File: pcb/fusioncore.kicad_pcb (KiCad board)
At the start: 2 copper layers, 95 x 99 mm, 107 parts, among them J1 Conn_02x12_Top_Bottom, J10 Pump_Misc_1, J11 Pump_Misc_2, J12 Flow_Warm, J13 Flow_Cold, J14 Trigger, J15 Valve_M1, J16 Valve_M2, J17 Valve_M3, J18 Valve_M4, J19 Valve_Air_Lime, J2 Temp_1, J20 Valve_Air_Rum, J21 Valve_Air_Out, J22 LED, J3 40HAT, J4 Temp_2, J5 WEIGHT, J6 Pump_Water_Cold, J7 Pump_Water_Warm, J8 Pump_Air, J9 CONN_01X02, Q1 DMG2305UX, Q10 AO3400A, Q11 AO3400A, Q12 AO3400A, Q13 AO3400A, Q14 AO3400A, Q15 BSS138, Q16 S8550, Q17 AO3400A, Q18 AO3400A, Q2 DMMT5401, Q3 AO3400A, Q4 AO3400A, Q5 AO3400A, Q6 AO3400A, Q7 AO3400A, Q8 AO3400A, Q9 AO3400A, U1 HX711, U2 CAT24C32, U3 LTC2990, U4 LTC2990

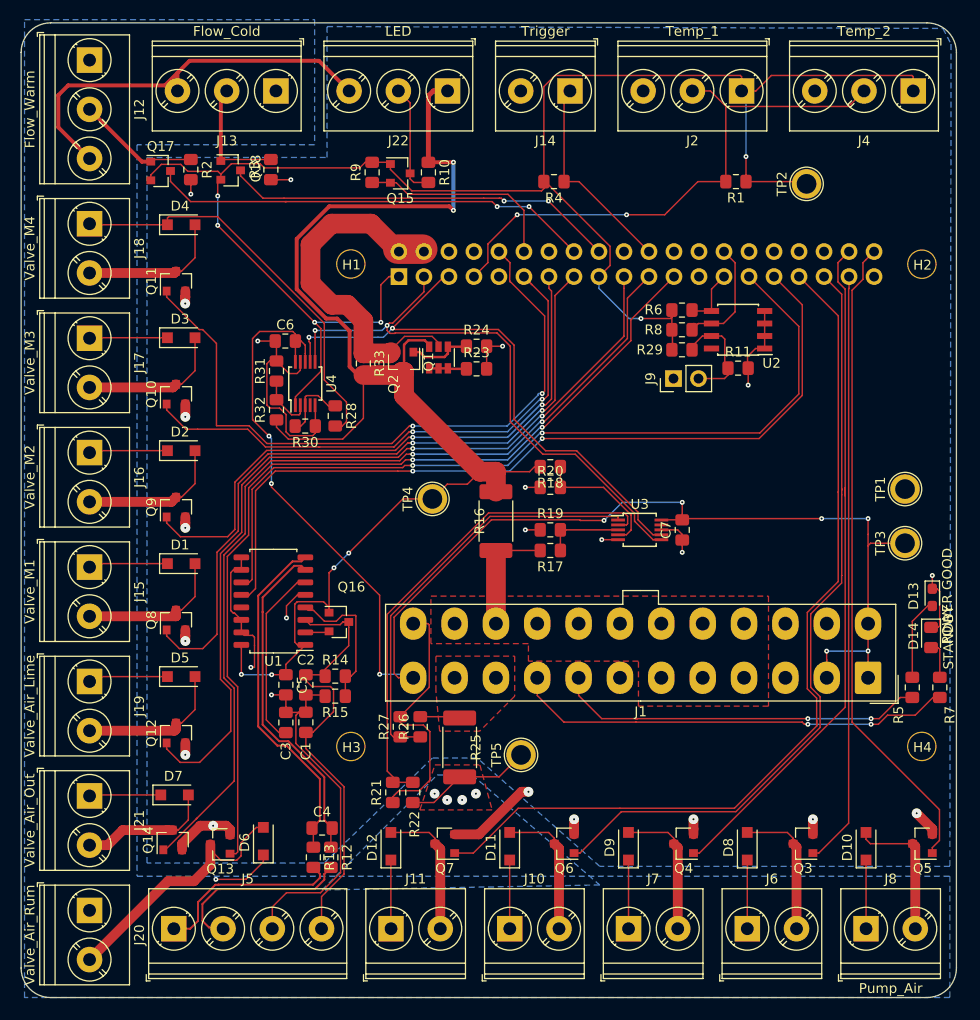
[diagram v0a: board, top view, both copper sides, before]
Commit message: Increased the number of vias for 12V power supply
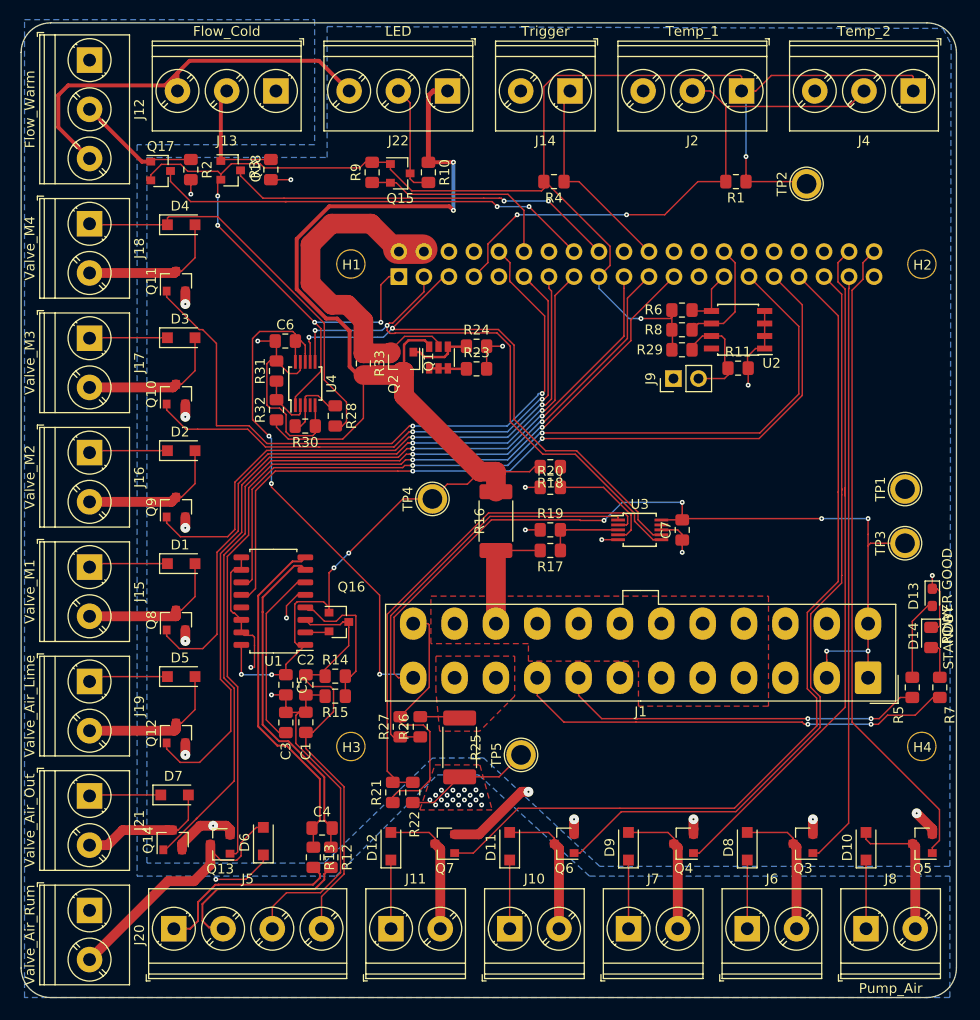
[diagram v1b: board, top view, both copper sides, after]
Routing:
- net /12V: vias 5 -> 20
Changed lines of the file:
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@@
     (thickness 1.6)
     (drawings 53)
-    (tracks 1091)
+    (tracks 1101)
     (zones 0)
     (modules 107)
@@
   )
   (page A4)
+  (title_block
+    (title "FusionCore Expansion")
+    (date 04.01.2020)
+    (rev A)
+    (company JKO)
+  )
   (layers
     (0 F.Cu signal)
-    (31 B.Cu signal hide)
+    (31 B.Cu signal)
     (32 B.Adhes user)
     (33 F.Adhes user)
@@
     (pad_to_mask_clearance 0.1)
     (aux_axis_origin 0 0)
-    (grid_origin 60.325 52.1716)
     (visible_elements 7FFFFE3F)
     (pcbplotparams
-      (layerselection 0x010f8_80000007)
+      (layerselection 0x010f0_ffffffff)
       (usegerberextensions false)
       (usegerberattributes false)
@@
       (drillshape 0)
       (scaleselection 1)
-      (outputdirectory "prod"))
+      (outputdirectory "gerber"))
   )
   (net 0 "")
@@
   (segment (start 72.252489 102.224489) (end 72.252489 103.063569) (width 0.15) (layer F.Cu) (net 1))
   (segment (start 72.252489 103.063569) (end 72.252489 105.283) (width 0.15) (layer F.Cu) (net 1))
-  (segment (start 65.228 101.480108) (end 65.228 102.080108) (width 1) (layer F.Cu) (net 1))
-  (segment (start 65.228 102.080108) (end 65.228 102.6025) (width 1) (layer F.Cu) (net 1))
   (segment (start 65.228 102.6025) (end 65.228 102.6025) (width 1) (layer F.Cu) (net 1))
   (via (at 65.228 102.6025) (size 1) (drill 0.2) (layers F.Cu B.Cu) (net 1))
-  (segment (start 65.228 90.00722) (end 65.228 90.60722) (width 1) (layer F.Cu) (net 1))
-  (segment (start 65.228 90.60722) (end 65.228 91.109) (width 1) (layer F.Cu) (net 1))
   (segment (start 65.228 91.109) (end 65.228 91.109) (width 1) (layer F.Cu) (net 1))
   (via (at 65.228 91.109) (size 1) (drill 0.2) (layers F.Cu B.Cu) (net 1))
@@
   (segment (start 65.228 79.833) (end 65.228 79.833) (width 1) (layer F.Cu) (net 1))
   (via (at 65.228 79.833) (size 1) (drill 0.2) (layers F.Cu B.Cu) (net 1))
-  (segment (start 65.228 67.661444) (end 65.2145 67.674944) (width 1) (layer F.Cu) (net 1))
-  (segment (start 65.2145 67.674944) (end 65.2145 68.326) (width 1) (layer F.Cu) (net 1))
-  (segment (start 65.228 67.061444) (end 65.228 67.661444) (width 1) (layer F.Cu) (net 1))
-  (segment (start 65.2145 68.326) (end 65.2145 68.326) (width 1) (layer F.Cu) (net 1))
-  (via (at 65.2145 68.326) (size 1) (drill 0.2) (layers F.Cu B.Cu) (net 1))
+  (via (at 65.2272 68.3768) (size 1) (drill 0.2) (layers F.Cu B.Cu) (net 1))
   (segment (start 74.614 55.748) (end 74.619 55.753) (width 0.15) (layer F.Cu) (net 1))
   (segment (start 73.914 55.748) (end 74.614 55.748) (width 0.15) (layer F.Cu) (net 1))
@@
   (segment (start 52.325 50.427) (end 55.499 53.601) (width 0.4) (layer F.Cu) (net 1))
   (segment (start 63.156923 46.1716) (end 53.325 46.1716) (width 0.4) (layer F.Cu) (net 1))
+  (segment (start 65.228 67.061444) (end 65.228 68.3776) (width 1) (layer F.Cu) (net 1))
+  (segment (start 65.228 91.109) (end 65.228 90.00722) (width 1) (layer F.Cu) (net 1))
+  (segment (start 65.228 102.6025) (end 65.228 101.480108) (width 1) (layer F.Cu) (net 1))
   (segment (start 119.94 66.06) (end 119.94 65.59) (width 0.25) (layer B.Cu) (net 2) (status 30))
   (segment (start 116.965 69.184) (end 116.77 68.989) (width 0.15) (layer F.Cu) (net 2) (status 30))
@@
   (segment (start 87.325 88.1716) (end 90.325 88.1716) (width 0.15) (layer F.Cu) (net 8))
   (segment (start 81.825 93.6716) (end 87.325 88.1716) (width 0.15) (layer F.Cu) (net 8))
-  (via (at 90.551 118.11) (size 1) (drill 0.2) (layers F.Cu B.Cu) (net 9))
-  (via (at 91.821 118.745) (size 1) (drill 0.2) (layers F.Cu B.Cu) (net 9))
-  (via (at 93.345 118.745) (size 1) (drill 0.2) (layers F.Cu B.Cu) (net 9))
-  (via (at 94.742 118.11) (size 1) (drill 0.2) (layers F.Cu B.Cu) (net 9))
-  (segment (start 90.4815 119.008) (end 93.091 116.3985) (width 0.15) (layer F.Cu) (net 9))
-  (segment (start 88.3285 119.008) (end 90.4815 119.008) (width 0.15) (layer F.Cu) (net 9))
   (segment (start 134.366 125.547) (end 134.366 131.826) (width 0.15) (layer F.Cu) (net 9))
   (segment (start 134.366 124.847) (end 134.366 125.547) (width 0.15) (layer F.Cu) (net 9))
@@
   (segment (start 63.538001 59.499999) (end 63.413 59.625) (width 0.15) (layer F.Cu) (net 9))
   (segment (start 68.51032 59.499999) (end 63.538001 59.499999) (width 0.15) (layer F.Cu) (net 9))
-  (segment (start 97.0981 116.3985) (end 99.325 114.1716) (width 0.15) (layer F.Cu) (net 9))
-  (segment (start 93.091 116.3985) (end 97.0981 116.3985) (width 0.15) (layer F.Cu) (net 9))
+  (via (at 95.3262 119.253) (size 0.5) (drill 0.2) (layers F.Cu B.Cu) (net 9))
+  (via (at 94.742 118.745) (size 0.5) (drill 0.2) (layers F.Cu B.Cu) (net 9))
+  (via (at 94.1578 119.253) (size 0.5) (drill 0.2) (layers F.Cu B.Cu) (net 9))
+  (via (at 93.5736 118.745) (size 0.5) (drill 0.2) (layers F.Cu B.Cu) (net 9))
+  (via (at 92.9894 119.253) (size 0.5) (drill 0.2) (layers F.Cu B.Cu) (net 9))
+  (via (at 92.4052 118.745) (size 0.5) (drill 0.2) (layers F.Cu B.Cu) (net 9))
+  (via (at 91.821 119.253) (size 0.5) (drill 0.2) (layers F.Cu B.Cu) (net 9))
+  (via (at 91.2368 118.745) (size 0.5) (drill 0.2) (layers F.Cu B.Cu) (net 9))
+  (via (at 90.6526 119.253) (size 0.5) (drill 0.2) (layers F.Cu B.Cu) (net 9))
+  (via (at 90.0684 118.745) (size 0.5) (drill 0.2) (layers F.Cu B.Cu) (net 9))
+  (via (at 94.1578 118.2624) (size 0.5) (drill 0.2) (layers F.Cu B.Cu) (net 9))
+  (via (at 92.9894 118.2624) (size 0.5) (drill 0.2) (layers F.Cu B.Cu) (net 9))
+  (via (at 91.821 118.2624) (size 0.5) (drill 0.2) (layers F.Cu B.Cu) (net 9))
+  (via (at 90.6526 118.2624) (size 0.5) (drill 0.2) (layers F.Cu B.Cu) (net 9))
+  (via (at 91.2368 117.7544) (size 0.5) (drill 0.2) (layers F.Cu B.Cu) (net 9))
+  (via (at 92.4052 117.7544) (size 0.5) (drill 0.2) (layers F.Cu B.Cu) (net 9))
+  (via (at 93.5736 117.729) (size 0.5) (drill 0.2) (layers F.Cu B.Cu) (net 9))
+  (via (at 94.742 117.729) (size 0.5) (drill 0.2) (layers F.Cu B.Cu) (net 9))
+  (via (at 95.3262 118.2624) (size 0.5) (drill 0.2) (layers F.Cu B.Cu) (net 9))
+  (segment (start 90.4815 119.008) (end 93.091 116.3985) (width 0.15) (layer F.Cu) (net 9))
+  (segment (start 88.3285 119.008) (end 90.4815 119.008) (width 0.15) (layer F.Cu) (net 9))
+  (segment (start 97.0981 116.3985) (end 93.091 116.3985) (width 0.15) (layer F.Cu) (net 9))
+  (segment (start 99.325 114.1716) (end 97.0981 116.3985) (width 0.15) (layer F.Cu) (net 9))
   (via (at 68.516001 57.404) (size 0.5) (drill 0.2) (layers F.Cu B.Cu) (net 10))
   (via (at 111.506 69.85) (size 0.5) (drill 0.2) (layers F.Cu B.Cu) (net 10))
@@
     (connect_pads (clearance 0.4))
     (min_thickness 0.254)
-    (fill yes (arc_segments 32) (thermal_gap 0.508) (thermal_bridge_width 0.508) (smoothing fillet) (radius 2))
-    (polygon
-      (pts
-        (xy 78.359 52.197) (xy 60.325 52.197) (xy 60.325 126.492) (xy 142.875 126.492) (xy 142.875 138.811)
-        (xy 48.895 138.811) (xy 48.895 39.497) (xy 78.359 39.497)
-      )
-    )
-  )
-  (zone (net 9) (net_name /12V) (layer B.Cu) (hatch edge 0.508)
-    (connect_pads (clearance 0.4))
-    (min_thickness 0.254)
     (fill yes (arc_segments 32) (thermal_gap 0.508) (thermal_bridge_width 0.508) (smoothing fillet) (radius 1))
     (polygon
       (pts
-        (xy 107.315 127.381) (xy 79.121 127.889) (xy 90.805 116.205) (xy 94.361 116.205)
+        (xy 78.359 52.197) (xy 60.325 52.197) (xy 60.325 126.492) (xy 80.518 126.492) (xy 90.805 116.205)
+        (xy 95.0214 116.205) (xy 106.284568 126.492) (xy 142.875 126.492) (xy 142.875 138.811) (xy 48.895 138.811)
+        (xy 48.895 39.497) (xy 78.359 39.497)
       )
     )
@@
     (polygon
       (pts
-        (xy 143.002 41.9735) (xy 142.875 125.492) (xy 107.325 125.492) (xy 94.875 114.492) (xy 90.325 114.492)
+        (xy 143.002 41.9735) (xy 142.875 125.492) (xy 107.325 125.492) (xy 95.5294 114.4778) (xy 90.325 114.492)
         (xy 79.325 125.1585) (xy 61.325 125.158497) (xy 61.325 53.492) (xy 79.629 53.492) (xy 79.629 40.1955)
         (xy 142.1765 40.386)

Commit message: Fixed component sizes and rearranged components to match spec
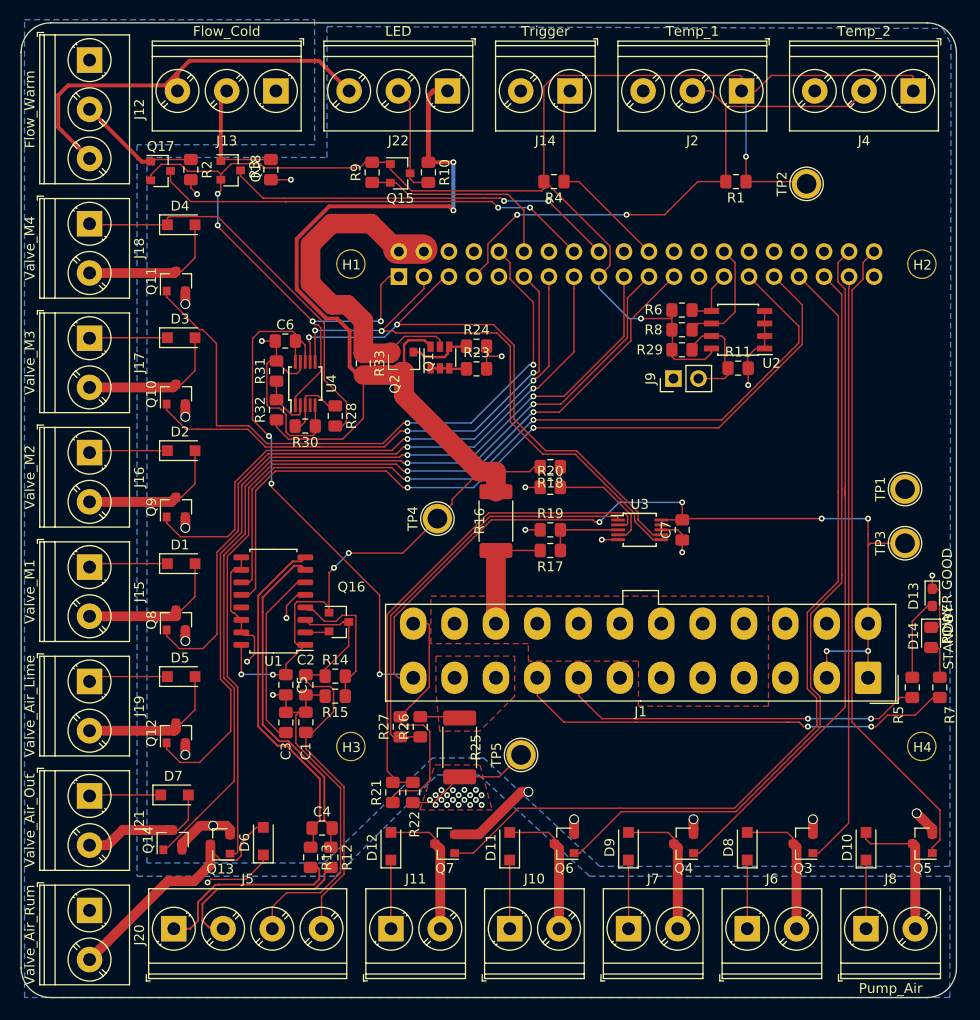
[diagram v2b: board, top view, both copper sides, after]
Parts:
- moved TP4 2.06 mm to (90.8, 90.2)
- moved R13 0.28 mm to (78.0, 124.6)
- moved Q2 0.14 mm to (91.1, 73.8)
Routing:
- net /3V3_PI: track 182.3 -> 188.7 mm
- net /Valve_M3: track 57.4 -> 53.5 mm
- net /Valve_M4: track 68.5 -> 65.2 mm
- net /Valve_M2: track 61.4 -> 59.1 mm
- net /Weight_CLK: track 83.9 -> 81.9 mm
- net /Valve_M1: track 72.1 -> 70.4 mm
- net /Weight_D: track 84.4 -> 82.8 mm
- net /12V: track 134.9 -> 135.9 mm
- net /5V_PI: track 37.1 -> 37.8 mm
- net /Valve_AR: track 92.5 -> 93.1 mm
- net /INA_C+: track 19.4 -> 19.9 mm
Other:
- net class Default: via_dia 0.5 -> 0.6; via_drill 0.2 -> 0.3
- rule via_min_drill: 0.2 -> 0.3
- rule via_min_size: 0.4 -> 0.6

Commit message: Minor PCB fixes.
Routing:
- net /3V3: track 145.4 -> 142.7 mm, vias 9 -> 7
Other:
- rule pad_to_mask_clearance: 0.1 -> 0.08

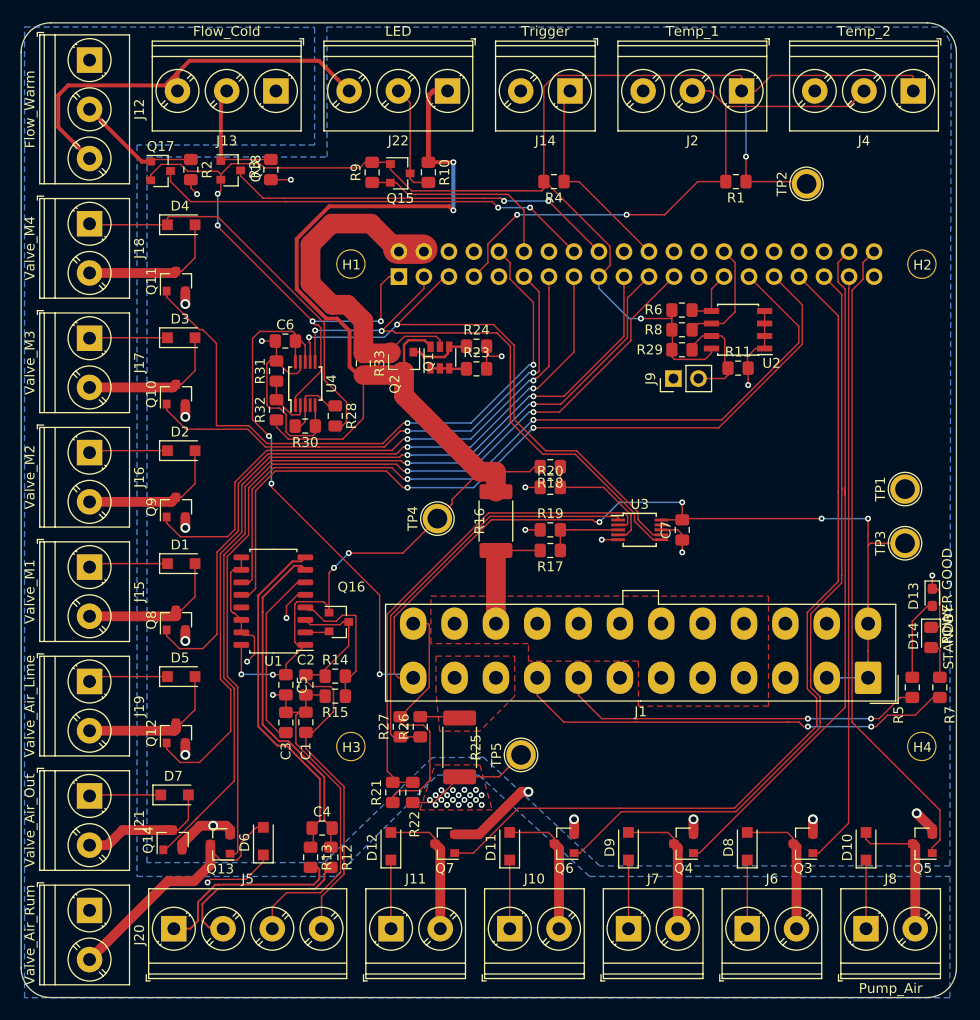
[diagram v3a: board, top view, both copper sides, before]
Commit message: Working on replacing some 2-Port Valves
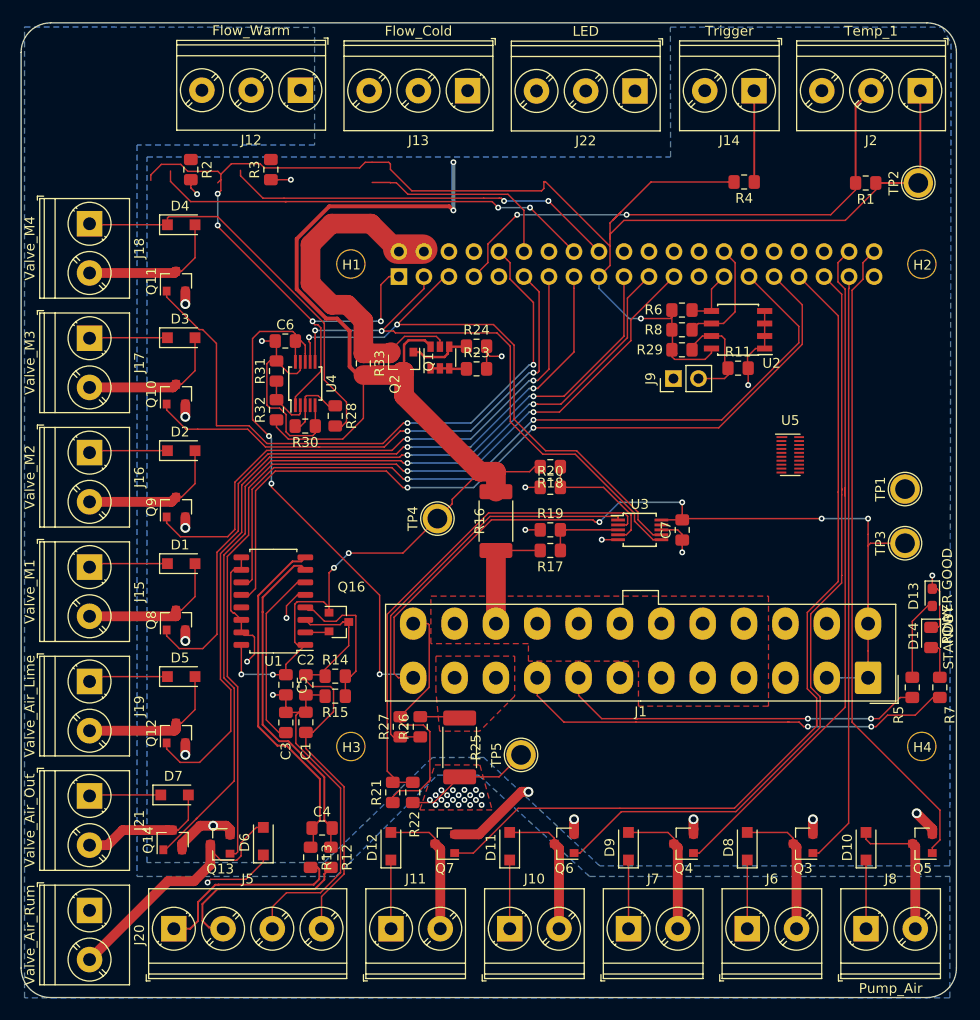
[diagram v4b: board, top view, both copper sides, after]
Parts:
- removed J4: Temp_2, TerminalBlock_Phoenix:TerminalBlock_Phoenix_PT-1,5-3-5.0-H_1x03_P5.00mm_Horizontal
- removed Q15: BSS138, Package_TO_SOT_SMD:SOT-23
- removed Q17, Q18: AO3400A, Package_TO_SOT_SMD:SOT-23
- removed R10, R9: 10K, Resistor_SMD:R_0805_2012Metric_Pad1.15x1.40mm_HandSolder
- added U5: TXB0108DQSR, Package_SON:USON-20_2x4mm_P0.4mm, F.Cu at (126.7, 83.7)
- Q16: value S8550 -> MMBT4403
- moved J12 21.6 mm to (76.9, 46.7), turned to 180 degrees
- moved J13 19.5 mm to (93.9, 46.7)
- moved R4 19.3 mm to (122.0, 56.0)
- moved J22 19.0 mm to (110.9, 46.7)
- moved J14 18.7 mm to (123.0, 46.7)
- moved J2 18.2 mm to (139.9, 46.7)
- moved R1 13.2 mm to (134.3, 56.1)
- moved TP2 11.3 mm to (139.7, 56.1)
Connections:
- net Net-(J12-Pad2) renamed /Flow_W_5V
- net Net-(J13-Pad2) renamed /Flow_C_5V
- J12 pad 1: /12V -> /5V
- J13 pad 1: /12V -> /5V
- J22 pad 2: Net-(J22-Pad2) -> /LED_PWM_5V
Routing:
- net GND: track 209.8 -> 168.0 mm
- net /Flow_W_5V: track 12.6 -> 0.00 mm
- net /Flow_C_5V: track 12.5 -> 0.00 mm
- net /Trigger: track 21.0 -> 9.28 mm
- net /5V: track 143.6 -> 132.2 mm
- net Net-(J22-Pad2): track 11.4 -> 0.00 mm
- net /3V3_PI: track 188.7 -> 183.3 mm, vias 6 -> 5
- net /1W: track 57.1 -> 54.2 mm
